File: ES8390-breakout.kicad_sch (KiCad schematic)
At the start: 65 parts, among them CN1 Conn_01x14_Pin, CN2 PJ-327A, CN3 PJ-327A, J1 PJ-603A, J2 Conn_01x02_Pin, J3 Conn_01x02_Pin, U1 TLV9062, U2 LP5907MFX-3.0, U3 ES8390, U4 IM68A130AXTMA1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

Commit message: first layout done
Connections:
- net ADOUT/AD1: now also CN1.6 (Pin_6); no longer CN1.10 (Pin_10)
- net CCLK: now also CN1.11 (Pin_11); no longer CN1.12 (Pin_12)
- net CDATA: now also CN1.12 (Pin_12); no longer CN1.11 (Pin_11)
- net DSDIN: now also CN1.8 (Pin_8); no longer CN1.9 (Pin_9)
- net LRCK: now also CN1.7 (Pin_7); no longer CN1.8 (Pin_8)
- net MCLK: now also CN1.10 (Pin_10), U3.1 (MCLK/DMIC_SCL/TDMIN); no longer CN1.6 (Pin_6)
- net SCLK: now also CN1.9 (Pin_9); no longer CN1.7 (Pin_7)

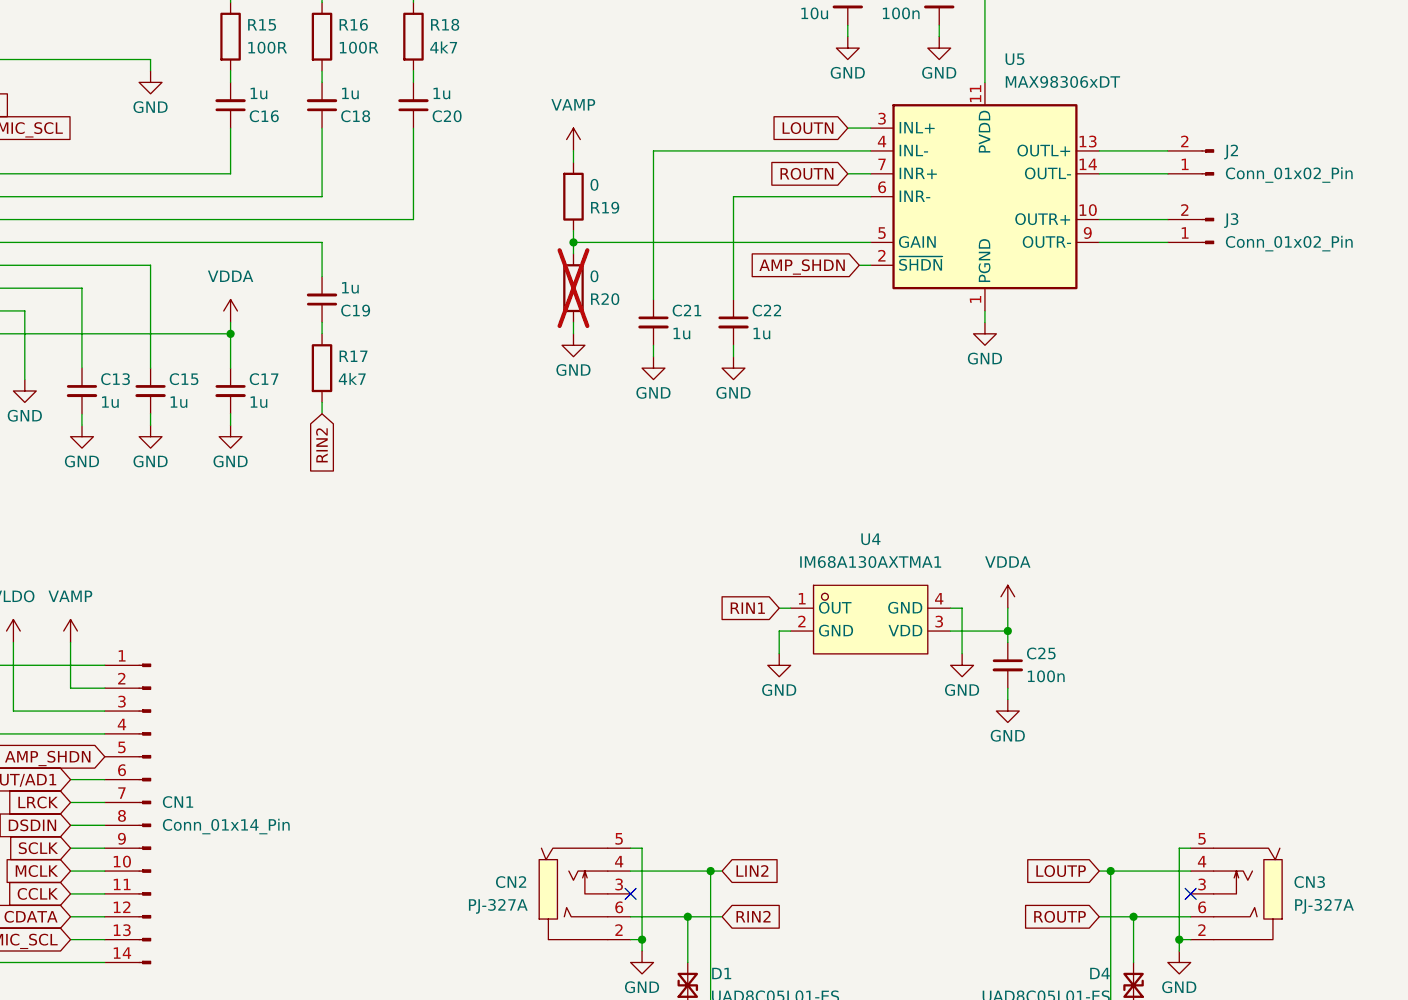
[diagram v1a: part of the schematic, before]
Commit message: replace microphone with top port MEMS MSM381ACP003
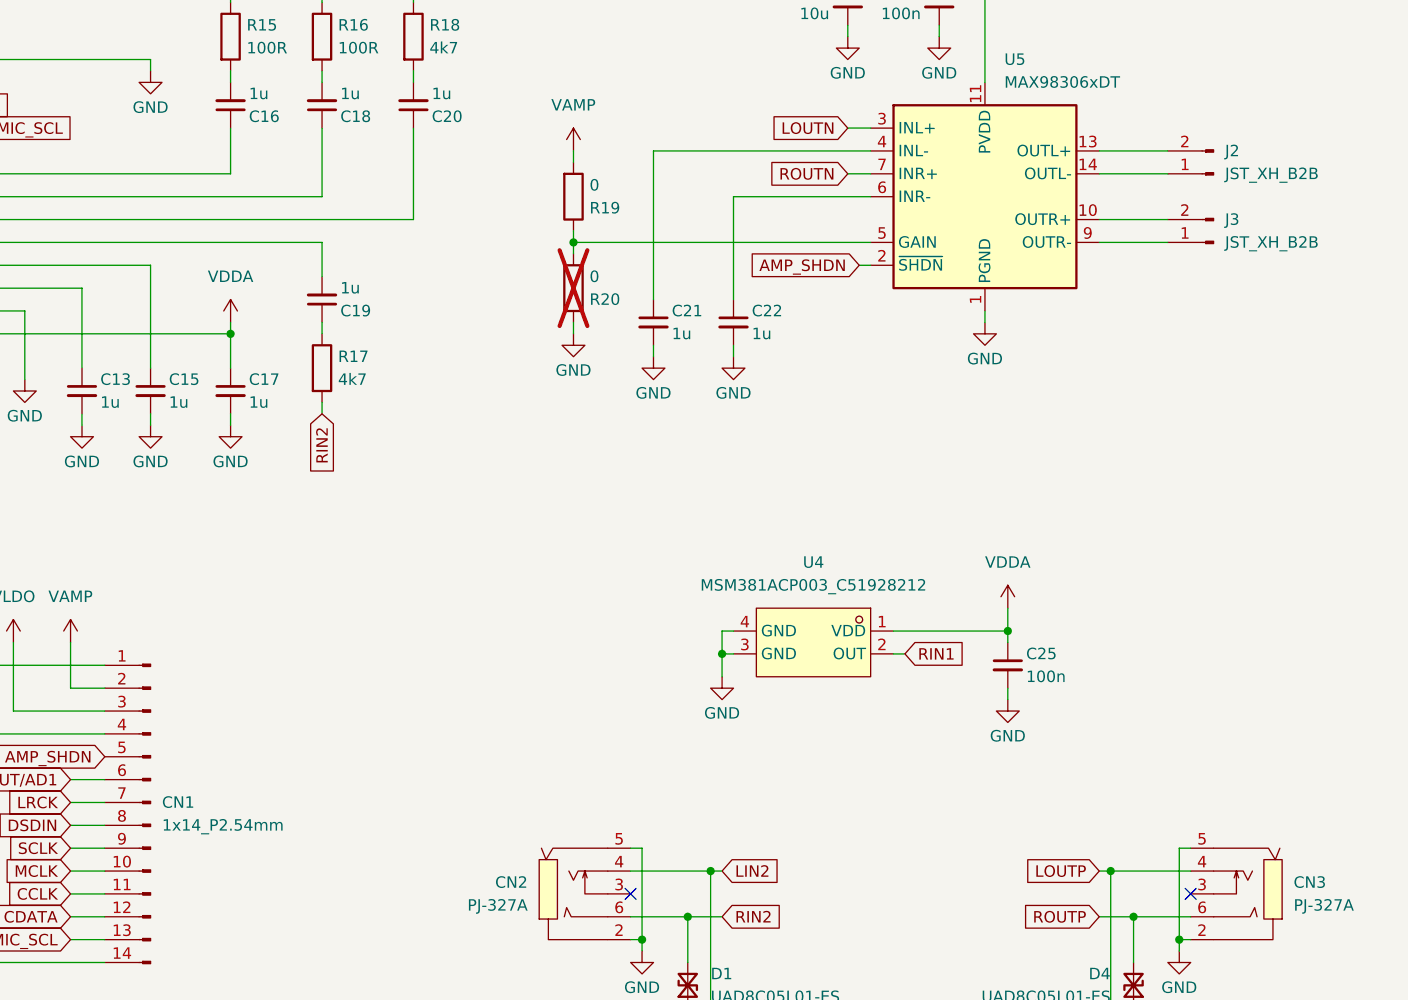
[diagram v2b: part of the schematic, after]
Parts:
- removed U4: IM68A130AXTMA1, lcsc:MIC-SMD_4P-L3.4-W2.5_IM68A130V01, symbol LCSC:IM68A130AXTMA1
- added U4: MSM381ACP003_C51928212, lcsc:MIC-SMD_4P-L2.8-W1.9-TR_MSM381ACP003, symbol LCSC:MSM381ACP003_C51928212
- CN1: value Conn_01x14_Pin -> 1x14_P2.54mm
- D1, D2, D3, D4: LCSC Part (none) -> C5199205
- J2, J3: value Conn_01x02_Pin -> JST_XH_B2B
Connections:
- net GND: now also U4.3 (GND), U4.4 (GND)
- net RIN1: now also U4.2 (OUT)
- net VDDA: now also U4.1 (VDD)

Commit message: v0.1 ordered pcb and components
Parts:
- R12, R13: LCSC Part C98220 -> C2906982
- U2: LCSC Part C2860052 -> C23380873
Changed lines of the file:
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@@
 			)
 		)
-		(property "LCSC Part" "C2860052"
+		(property "LCSC Part" "C23380873"
 			(at 50.8 120.65 0)
 			(hide yes)
@@
 			)
 		)
-		(property "LCSC Part" "C98220"
+		(property "LCSC Part" "C2906982"
 			(at 102.87 172.72 0)
 			(hide yes)
@@
 			)
 		)
-		(property "LCSC Part" "C98220"
+		(property "LCSC Part" "C2906982"
 			(at 113.03 167.64 0)
 			(hide yes)
